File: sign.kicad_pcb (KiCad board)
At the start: 2 copper layers, 1 part

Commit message: Route 'e'
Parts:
- removed REF**: APA102C_72m_x3, apa102c_72m:APA102C_72m_x3
- added J1, J2, J3: CONN_01X02, Pin_Headers:Pin_Header_Straight_1x02, F.Cu at (28.2, 196.5)
- added U1: APA102C_x6, apa102c_72m:APA102C_72m_x6, B.Cu at (51.7, 204.4)
- added U10: APA102C_x2, apa102c_72m:APA102C_72m_x2, B.Cu at (121.1, 190.6)
- added U100: APA102C_x6, apa102c_72m:APA102C_72m_x6, B.Cu at (551.7, 79.4)
- added U101: APA102C_x4, apa102c_72m:APA102C_72m_x4, B.Cu at (551.7, 315.6)
- added U102: APA102C_x2, apa102c_72m:APA102C_72m_x2, B.Cu at (551.7, 593.3)
- added U103: APA102C_x1, apa102c_72m:APA102C_72m_x1, B.Cu at (565.6, 44.7)
- added U104: APA102C_x3, apa102c_72m:APA102C_72m_x3, B.Cu at (565.6, 322.5)
- added U105: APA102C_x5, apa102c_72m:APA102C_72m_x5, B.Cu at (565.6, 572.5)
- added U106: APA102C_x2, apa102c_72m:APA102C_72m_x2, B.Cu at (579.4, 135.0)
- added U107: APA102C_x3, apa102c_72m:APA102C_72m_x3, B.Cu at (579.4, 322.5)
- added U108: APA102C_x10, apa102c_72m:APA102C_72m_x10, B.Cu at (579.4, 537.8)
- added U109: APA102C_x9, apa102c_72m:APA102C_72m_x9, B.Cu at (593.3, 169.7)
- added U11: APA102C_x2, apa102c_72m:APA102C_72m_x2, B.Cu at (121.1, 260.0)
- added U110: APA102C_x3, apa102c_72m:APA102C_72m_x3, B.Cu at (593.3, 308.6)
- added U111: APA102C_x12, apa102c_72m:APA102C_72m_x12, B.Cu at (593.3, 523.9)
- added U112: APA102C_x16, apa102c_72m:APA102C_72m_x16, B.Cu at (607.2, 218.3)
- added U113: APA102C_x8, apa102c_72m:APA102C_72m_x8, B.Cu at (607.2, 496.1)
- added U114: APA102C_x13, apa102c_72m:APA102C_72m_x13, B.Cu at (621.1, 225.3)
- added U115: APA102C_x3, apa102c_72m:APA102C_72m_x3, B.Cu at (621.1, 489.2)
- added U116: APA102C_x6, apa102c_72m:APA102C_72m_x6, B.Cu at (635.0, 246.1)
- added U117: APA102C_x3, apa102c_72m:APA102C_72m_x3, B.Cu at (635.0, 475.3)
- added U118: APA102C_x6, apa102c_72m:APA102C_72m_x6, B.Cu at (648.9, 218.3)
- added U119: APA102C_x3, apa102c_72m:APA102C_72m_x3, B.Cu at (648.9, 461.4)
- added U12: APA102C_x2, apa102c_72m:APA102C_72m_x2, B.Cu at (135.0, 121.1)
- added U120: APA102C_x2, apa102c_72m:APA102C_72m_x2, B.Cu at (648.9, 593.3)
- added U121: APA102C_x6, apa102c_72m:APA102C_72m_x6, B.Cu at (662.8, 190.6)
- added U122: APA102C_x3, apa102c_72m:APA102C_72m_x3, B.Cu at (662.8, 461.4)
- added U123: APA102C_x6, apa102c_72m:APA102C_72m_x6, B.Cu at (662.8, 565.6)
- added U124: APA102C_x7, apa102c_72m:APA102C_72m_x7, B.Cu at (676.7, 169.7)
- added U125: APA102C_x12, apa102c_72m:APA102C_72m_x12, B.Cu at (676.7, 523.9)
- added U126: APA102C_x6, apa102c_72m:APA102C_72m_x6, B.Cu at (690.6, 148.9)
- added U127: APA102C_x11, apa102c_72m:APA102C_72m_x11, B.Cu at (690.6, 516.9)
- added U128: APA102C_x4, apa102c_72m:APA102C_72m_x4, B.Cu at (704.4, 135.0)
- added U129: APA102C_x6, apa102c_72m:APA102C_72m_x6, B.Cu at (704.4, 496.1)
- added U13: APA102C_x2, apa102c_72m:APA102C_72m_x2, B.Cu at (135.0, 190.6)
- added U130: APA102C_x2, apa102c_72m:APA102C_72m_x2, B.Cu at (718.3, 121.1)
- added U131: APA102C_x2, apa102c_72m:APA102C_72m_x2, B.Cu at (718.3, 482.2)
- added U132: APA102C_x3, apa102c_72m:APA102C_72m_x3, B.Cu at (732.2, 475.3)
- added U133: APA102C_x1, apa102c_72m:APA102C_72m_x1, B.Cu at (732.2, 600.3)
- added U134: APA102C_x3, apa102c_72m:APA102C_72m_x3, B.Cu at (746.1, 461.4)
- added U135: APA102C_x3, apa102c_72m:APA102C_72m_x3, B.Cu at (746.1, 586.4)
- added U136: APA102C_x12, apa102c_72m:APA102C_72m_x12, B.Cu at (760.0, 523.9)
- added U137: APA102C_x12, apa102c_72m:APA102C_72m_x12, B.Cu at (773.9, 523.9)
- added U138: APA102C_x9, apa102c_72m:APA102C_72m_x9, B.Cu at (787.8, 516.9)
- added U139: APA102C_x4, apa102c_72m:APA102C_72m_x4, B.Cu at (801.7, 496.1)
- added U14: APA102C_x3, apa102c_72m:APA102C_72m_x3, B.Cu at (135.0, 253.1)
- added U15: APA102C_x3, apa102c_72m:APA102C_72m_x3, B.Cu at (148.9, 128.1)
- added U16: APA102C_x3, apa102c_72m:APA102C_72m_x3, B.Cu at (148.9, 183.6)
- added U17: APA102C_x3, apa102c_72m:APA102C_72m_x3, B.Cu at (148.9, 253.1)
- added U18: APA102C_x5, apa102c_72m:APA102C_72m_x5, B.Cu at (148.9, 475.3)
- added U19: APA102C_x6, apa102c_72m:APA102C_72m_x6, B.Cu at (162.8, 148.9)
- added U2: APA102C_x8, apa102c_72m:APA102C_72m_x8, B.Cu at (65.6, 204.4)
- added U20: APA102C_x2, apa102c_72m:APA102C_72m_x2, B.Cu at (162.8, 246.1)
- added U21: APA102C_x7, apa102c_72m:APA102C_72m_x7, B.Cu at (162.8, 475.3)
- added U22: APA102C_x5, apa102c_72m:APA102C_72m_x5, B.Cu at (176.7, 155.8)
- added U23: APA102C_x7, apa102c_72m:APA102C_72m_x7, B.Cu at (176.7, 419.7)
- added U24: APA102C_x3, apa102c_72m:APA102C_72m_x3, B.Cu at (176.7, 503.1)
- added U25: APA102C_x2, apa102c_72m:APA102C_72m_x2, B.Cu at (190.6, 148.9)
- added U26: APA102C_x7, apa102c_72m:APA102C_72m_x7, B.Cu at (190.6, 405.8)
- added U27: APA102C_x2, apa102c_72m:APA102C_72m_x2, B.Cu at (190.6, 510.0)
- added U28: APA102C_x3, apa102c_72m:APA102C_72m_x3, B.Cu at (204.4, 364.2)
- added U29: APA102C_x5, apa102c_72m:APA102C_72m_x5, B.Cu at (204.4, 433.6)
- added U3: APA102C_x11, apa102c_72m:APA102C_72m_x11, B.Cu at (79.4, 197.5)
- added U30: APA102C_x2, apa102c_72m:APA102C_72m_x2, B.Cu at (204.4, 510.0)
- added U31: APA102C_x5, apa102c_72m:APA102C_72m_x5, B.Cu at (218.3, 211.4)
- added U32: APA102C_x2, apa102c_72m:APA102C_72m_x2, B.Cu at (218.3, 357.2)
- added U33: APA102C_x8, apa102c_72m:APA102C_72m_x8, B.Cu at (218.3, 468.3)
- added U34: APA102C_x9, apa102c_72m:APA102C_72m_x9, B.Cu at (232.2, 197.5)
- added U35: APA102C_x3, apa102c_72m:APA102C_72m_x3, B.Cu at (232.2, 364.2)
- added U36: APA102C_x2, apa102c_72m:APA102C_72m_x2, B.Cu at (232.2, 412.8)
- added U37: APA102C_x5, apa102c_72m:APA102C_72m_x5, B.Cu at (232.2, 475.3)
- added U38: APA102C_x11, apa102c_72m:APA102C_72m_x11, B.Cu at (246.1, 197.5)
- added U39: APA102C_x6, apa102c_72m:APA102C_72m_x6, B.Cu at (246.1, 385.0)
- added U4: APA102C_x6, apa102c_72m:APA102C_72m_x6, B.Cu at (93.3, 162.8)
- added U40: APA102C_x4, apa102c_72m:APA102C_72m_x4, B.Cu at (246.1, 496.1)
- added U41: APA102C_x5, apa102c_72m:APA102C_72m_x5, B.Cu at (260.0, 155.8)
- added U42: APA102C_x3, apa102c_72m:APA102C_72m_x3, B.Cu at (260.0, 253.1)
- added U43: APA102C_x4, apa102c_72m:APA102C_72m_x4, B.Cu at (260.0, 385.0)
- added U44: APA102C_x6, apa102c_72m:APA102C_72m_x6, B.Cu at (260.0, 482.2)
- added U45: APA102C_x4, apa102c_72m:APA102C_72m_x4, B.Cu at (273.9, 135.0)
- added U46: APA102C_x3, apa102c_72m:APA102C_72m_x3, B.Cu at (273.9, 253.1)
- added U47: APA102C_x4, apa102c_72m:APA102C_72m_x4, B.Cu at (273.9, 454.4)
- added U48: APA102C_x2, apa102c_72m:APA102C_72m_x2, B.Cu at (273.9, 510.0)
- added U49: APA102C_x3, apa102c_72m:APA102C_72m_x3, B.Cu at (287.8, 128.1)
- added U5: APA102C_x3, apa102c_72m:APA102C_72m_x3, B.Cu at (93.3, 253.1)
- added U50: APA102C_x2, apa102c_72m:APA102C_72m_x2, B.Cu at (287.8, 246.1)
- added U51: APA102C_x2, apa102c_72m:APA102C_72m_x2, B.Cu at (287.8, 440.6)
- added U52: APA102C_x3, apa102c_72m:APA102C_72m_x3, B.Cu at (301.7, 128.1)
- added U53: APA102C_x3, apa102c_72m:APA102C_72m_x3, B.Cu at (301.7, 239.2)
- added U54: APA102C_x3, apa102c_72m:APA102C_72m_x3, B.Cu at (301.7, 641.9)
- added U55: APA102C_x3, apa102c_72m:APA102C_72m_x3, B.Cu at (315.6, 141.9)
- added U56: APA102C_x7, apa102c_72m:APA102C_72m_x7, B.Cu at (315.6, 225.3)
- added U57: APA102C_x4, apa102c_72m:APA102C_72m_x4, B.Cu at (315.6, 648.9)
- added U58: APA102C_x12, apa102c_72m:APA102C_72m_x12, B.Cu at (329.4, 190.6)
- added U59: APA102C_x3, apa102c_72m:APA102C_72m_x3, B.Cu at (329.4, 655.8)
- added U6: APA102C_x3, apa102c_72m:APA102C_72m_x3, B.Cu at (107.2, 128.1)
- added U60: APA102C_x14, apa102c_72m:APA102C_72m_x14, B.Cu at (343.3, 148.9)
- added U61: APA102C_x3, apa102c_72m:APA102C_72m_x3, B.Cu at (343.3, 655.8)
- added U62: APA102C_x10, apa102c_72m:APA102C_72m_x10, B.Cu at (357.2, 107.2)
- added U63: APA102C_x4, apa102c_72m:APA102C_72m_x4, B.Cu at (357.2, 635.0)
- added U64: APA102C_x6, apa102c_72m:APA102C_72m_x6, B.Cu at (371.1, 79.4)
- added U65: APA102C_x9, apa102c_72m:APA102C_72m_x9, B.Cu at (371.1, 600.3)
- added U66: APA102C_x1, apa102c_72m:APA102C_72m_x1, B.Cu at (385.0, 44.7)
- added U67: APA102C_x13, apa102c_72m:APA102C_72m_x13, B.Cu at (385.0, 558.6)
- added U68: APA102C_x5, apa102c_72m:APA102C_72m_x5, B.Cu at (398.9, 211.4)
- added U69: APA102C_x13, apa102c_72m:APA102C_72m_x13, B.Cu at (398.9, 530.8)
- added U7: APA102C_x2, apa102c_72m:APA102C_72m_x2, B.Cu at (107.2, 190.6)
- added U70: APA102C_x9, apa102c_72m:APA102C_72m_x9, B.Cu at (412.8, 197.5)
- added U71: APA102C_x2, apa102c_72m:APA102C_72m_x2, B.Cu at (412.8, 398.9)
- added U72: APA102C_x8, apa102c_72m:APA102C_72m_x8, B.Cu at (412.8, 496.1)
- added U73: APA102C_x11, apa102c_72m:APA102C_72m_x11, B.Cu at (426.7, 197.5)
- added U74: APA102C_x3, apa102c_72m:APA102C_72m_x3, B.Cu at (426.7, 391.9)
- added U75: APA102C_x3, apa102c_72m:APA102C_72m_x3, B.Cu at (426.7, 461.4)
- added U76: APA102C_x5, apa102c_72m:APA102C_72m_x5, B.Cu at (440.6, 155.8)
- added U77: APA102C_x3, apa102c_72m:APA102C_72m_x3, B.Cu at (440.6, 253.1)
- added U78: APA102C_x2, apa102c_72m:APA102C_72m_x2, B.Cu at (440.6, 385.0)
- added U79: APA102C_x4, apa102c_72m:APA102C_72m_x4, B.Cu at (454.4, 135.0)
- added U8: APA102C_x3, apa102c_72m:APA102C_72m_x3, B.Cu at (107.2, 253.1)
- added U80: APA102C_x3, apa102c_72m:APA102C_72m_x3, B.Cu at (454.4, 253.1)
- added U81: APA102C_x2, apa102c_72m:APA102C_72m_x2, B.Cu at (454.4, 593.3)
- added U82: APA102C_x3, apa102c_72m:APA102C_72m_x3, B.Cu at (468.3, 128.1)
- added U83: APA102C_x2, apa102c_72m:APA102C_72m_x2, B.Cu at (468.3, 246.1)
- added U84: APA102C_x5, apa102c_72m:APA102C_72m_x5, B.Cu at (468.3, 572.5)
- added U85: APA102C_x3, apa102c_72m:APA102C_72m_x3, B.Cu at (482.2, 128.1)
- added U86: APA102C_x3, apa102c_72m:APA102C_72m_x3, B.Cu at (482.2, 239.2)
- added U87: APA102C_x10, apa102c_72m:APA102C_72m_x10, B.Cu at (482.2, 537.8)
- added U88: APA102C_x3, apa102c_72m:APA102C_72m_x3, B.Cu at (496.1, 141.9)
- added U89: APA102C_x7, apa102c_72m:APA102C_72m_x7, B.Cu at (496.1, 225.3)
- added U9: APA102C_x3, apa102c_72m:APA102C_72m_x3, B.Cu at (121.1, 128.1)
- added U90: APA102C_x12, apa102c_72m:APA102C_72m_x12, B.Cu at (496.1, 523.9)
- added U91: APA102C_x12, apa102c_72m:APA102C_72m_x12, B.Cu at (510.0, 190.6)
- added U92: APA102C_x2, apa102c_72m:APA102C_72m_x2, B.Cu at (510.0, 398.9)
- added U93: APA102C_x8, apa102c_72m:APA102C_72m_x8, B.Cu at (510.0, 496.1)
- added U94: APA102C_x14, apa102c_72m:APA102C_72m_x14, B.Cu at (523.9, 148.9)
- added U95: APA102C_x3, apa102c_72m:APA102C_72m_x3, B.Cu at (523.9, 391.9)
- added U96: APA102C_x3, apa102c_72m:APA102C_72m_x3, B.Cu at (523.9, 461.4)
- added U97: APA102C_x10, apa102c_72m:APA102C_72m_x10, B.Cu at (537.8, 107.2)
- added U98: APA102C_x3, apa102c_72m:APA102C_72m_x3, B.Cu at (537.8, 308.6)
- added U99: APA102C_x2, apa102c_72m:APA102C_72m_x2, B.Cu at (537.8, 385.0)
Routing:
- net Net-(U20-Pad8): track 0.00 -> 198.2 mm
- net Net-(U20-Pad7): track 0.00 -> 191.6 mm
- net Net-(U20-Pad6): track 0.00 -> 183.7 mm
- net Net-(U20-Pad5): track 0.00 -> 175.3 mm
- net Net-(U16-Pad4): track 0.00 -> 59.6 mm
- net Net-(U2-Pad5): track 0.00 -> 58.5 mm
- net Net-(U16-Pad3): track 0.00 -> 58.1 mm
- net Net-(U16-Pad2): track 0.00 -> 57.4 mm
- net Net-(U16-Pad1): track 0.00 -> 54.2 mm
- net Net-(U2-Pad6): track 0.00 -> 50.8 mm
- net Net-(U12-Pad8): track 0.00 -> 47.2 mm
- net Net-(U4-Pad5): track 0.00 -> 46.3 mm
- net Net-(U1-Pad8): track 0.00 -> 46.2 mm
- net Net-(U22-Pad5): track 0.00 -> 46.0 mm
- net Net-(U2-Pad7): track 0.00 -> 44.6 mm
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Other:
- net class Default: clearance 0.2 -> 0.6; trace_width 0.25 -> 2
- net class Signal added: clearance 0.6, trace_width 1, via_dia 0.6, via_drill 0.4
- rule trace_clearance: 0.2 -> 0.6

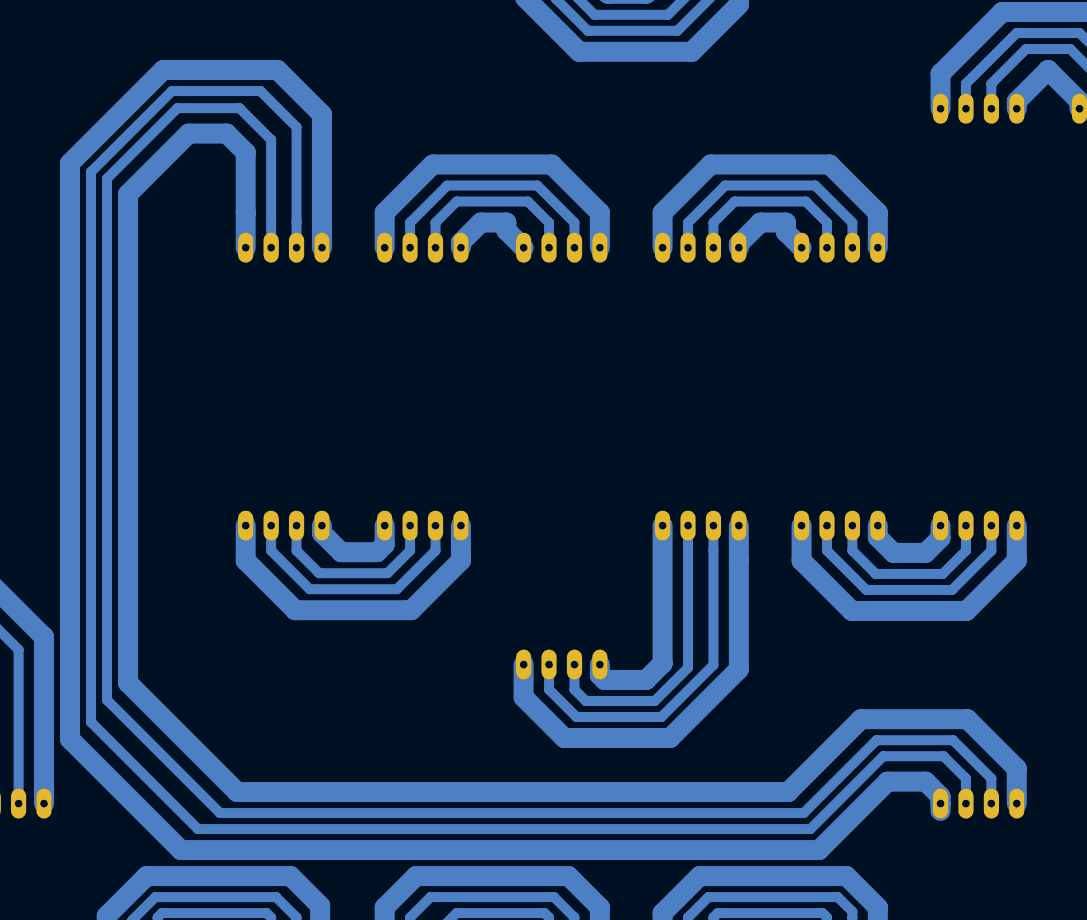
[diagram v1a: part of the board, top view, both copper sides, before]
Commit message: nets for 'i'
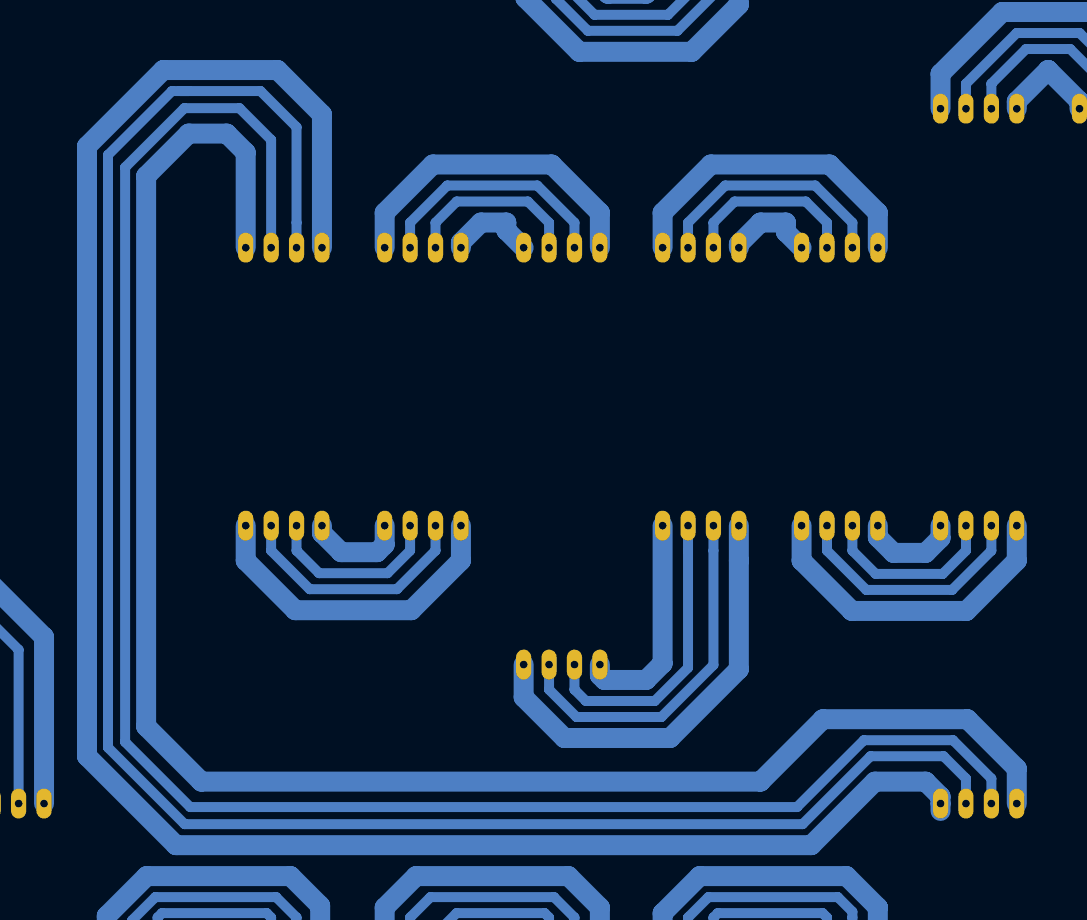
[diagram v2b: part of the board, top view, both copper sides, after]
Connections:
- U81 pad 5: (no net) -> Net-(U81-Pad5)
- U81 pad 6: (no net) -> Net-(U81-Pad6)
- U81 pad 7: (no net) -> Net-(U81-Pad7)
- U81 pad 8: (no net) -> Net-(U81-Pad8)
- U84 pad 1: (no net) -> Net-(U81-Pad5)
- U84 pad 2: (no net) -> Net-(U81-Pad6)
- U84 pad 3: (no net) -> Net-(U81-Pad7)
- U84 pad 4: (no net) -> Net-(U81-Pad8)
- U84 pad 5: (no net) -> Net-(U84-Pad5)
- U84 pad 6: (no net) -> Net-(U84-Pad6)
- U84 pad 7: (no net) -> Net-(U84-Pad7)
- U84 pad 8: (no net) -> Net-(U84-Pad8)
- U87 pad 1: (no net) -> Net-(U84-Pad5)
- U87 pad 2: (no net) -> Net-(U84-Pad6)
- U87 pad 3: (no net) -> Net-(U84-Pad7)
- U87 pad 4: (no net) -> Net-(U84-Pad8)
- U87 pad 5: (no net) -> Net-(U87-Pad5)
- U87 pad 6: (no net) -> Net-(U87-Pad6)
- U87 pad 7: (no net) -> Net-(U87-Pad7)
- U87 pad 8: (no net) -> Net-(U87-Pad8)
- U90 pad 1: (no net) -> Net-(U87-Pad5)
- U90 pad 2: (no net) -> Net-(U87-Pad6)
- U90 pad 3: (no net) -> Net-(U87-Pad7)
- U90 pad 4: (no net) -> Net-(U87-Pad8)
- U90 pad 5: (no net) -> Net-(U90-Pad5)
- U90 pad 6: (no net) -> Net-(U90-Pad6)
- U90 pad 7: (no net) -> Net-(U90-Pad7)
- U90 pad 8: (no net) -> Net-(U90-Pad8)
- U93 pad 1: (no net) -> Net-(U90-Pad5)
- U93 pad 2: (no net) -> Net-(U90-Pad6)
- U93 pad 3: (no net) -> Net-(U90-Pad7)
- U93 pad 4: (no net) -> Net-(U90-Pad8)
- U93 pad 5: (no net) -> Net-(U93-Pad5)
- U93 pad 6: (no net) -> Net-(U93-Pad6)
- U93 pad 7: (no net) -> Net-(U93-Pad7)
- U93 pad 8: (no net) -> Net-(U93-Pad8)
- U96 pad 1: (no net) -> Net-(U93-Pad5)
- U96 pad 2: (no net) -> Net-(U93-Pad6)
- U96 pad 3: (no net) -> Net-(U93-Pad7)
- U96 pad 4: (no net) -> Net-(U93-Pad8)
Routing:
- net Net-(U20-Pad8): track 198.2 -> 196.4 mm
- net Net-(U20-Pad7): track 191.6 -> 190.2 mm
- net Net-(U20-Pad6): track 183.7 -> 182.7 mm
- net Net-(U20-Pad5): track 175.3 -> 174.4 mm

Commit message: Add cuts layer.
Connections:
- J1 pad 1: +5V -> GND
- J1 pad 2: GND -> +5V
- U1 pad 1: +5V -> GND
- U1 pad 4: GND -> +5V
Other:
- board outline added: 767.9 x 642.9 mm

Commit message: Update edge cuts
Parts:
- moved J2 10.1 mm to (25.7, 206.2)
- moved J1 8.34 mm to (25.9, 188.5)

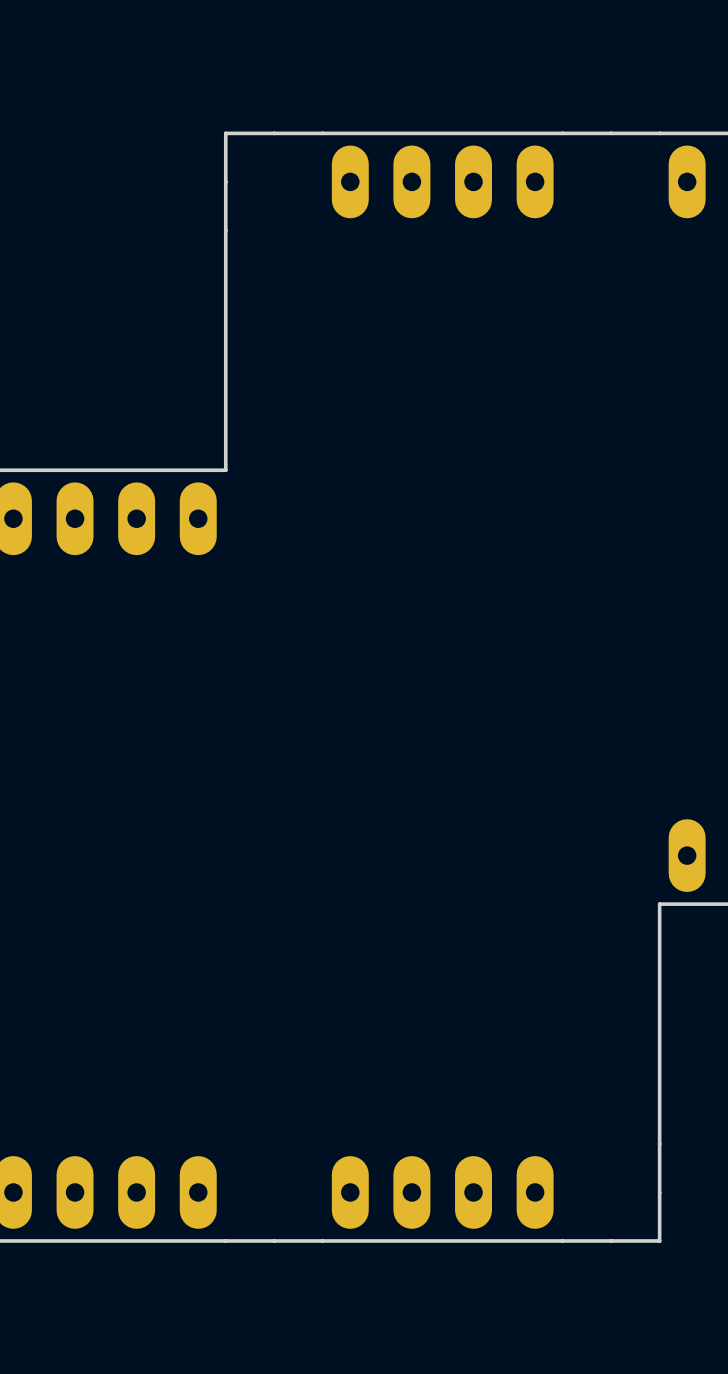
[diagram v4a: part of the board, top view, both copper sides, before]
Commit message: Wire up some more letters.
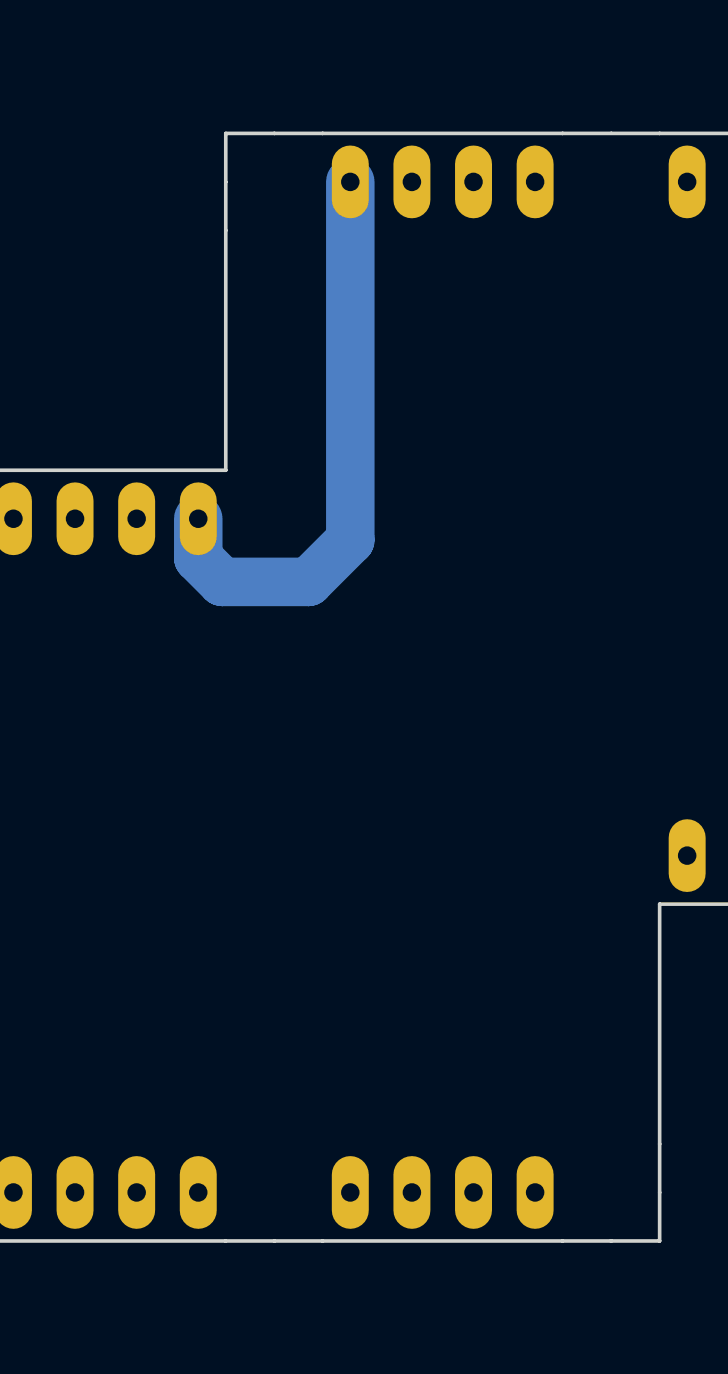
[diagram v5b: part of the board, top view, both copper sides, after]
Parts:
- turned U74 to 270 degrees
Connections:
- U100 pad 1: (no net) -> Net-(U100-Pad1)
- U100 pad 2: (no net) -> Net-(U100-Pad2)
- U100 pad 3: (no net) -> Net-(U100-Pad3)
- U100 pad 4: (no net) -> Net-(U100-Pad4)
- U100 pad 5: (no net) -> Net-(U100-Pad5)
- U100 pad 6: (no net) -> Net-(U100-Pad6)
- U100 pad 7: (no net) -> Net-(U100-Pad7)
- U100 pad 8: (no net) -> Net-(U100-Pad8)
- U103 pad 1: (no net) -> Net-(U100-Pad5)
- U103 pad 2: (no net) -> Net-(U100-Pad6)
- U103 pad 3: (no net) -> Net-(U100-Pad7)
- U103 pad 4: (no net) -> Net-(U100-Pad8)
- U103 pad 5: (no net) -> Net-(U103-Pad5)
- U103 pad 6: (no net) -> Net-(U103-Pad6)
- U103 pad 7: (no net) -> Net-(U103-Pad7)
- U103 pad 8: (no net) -> Net-(U103-Pad8)
- U31 pad 1: (no net) -> GND
- U31 pad 4: (no net) -> +5V
- U31 pad 5: (no net) -> Net-(U31-Pad5)
- U31 pad 6: (no net) -> Net-(U31-Pad6)
- U31 pad 7: (no net) -> Net-(U31-Pad7)
- U31 pad 8: (no net) -> Net-(U31-Pad8)
- U34 pad 1: (no net) -> Net-(U31-Pad5)
- U34 pad 2: (no net) -> Net-(U31-Pad6)
- U34 pad 3: (no net) -> Net-(U31-Pad7)
- U34 pad 4: (no net) -> Net-(U31-Pad8)
- U34 pad 5: (no net) -> Net-(U34-Pad5)
- U34 pad 6: (no net) -> Net-(U34-Pad6)
- U34 pad 7: (no net) -> Net-(U34-Pad7)
- U34 pad 8: (no net) -> Net-(U34-Pad8)
- U38 pad 1: (no net) -> Net-(U34-Pad5)
- U38 pad 2: (no net) -> Net-(U34-Pad6)
- U38 pad 3: (no net) -> Net-(U34-Pad7)
- U38 pad 4: (no net) -> Net-(U34-Pad8)
- U38 pad 5: (no net) -> Net-(U38-Pad5)
- U38 pad 6: (no net) -> Net-(U38-Pad6)
- U38 pad 7: (no net) -> Net-(U38-Pad7)
- U38 pad 8: (no net) -> Net-(U38-Pad8)
- U41 pad 1: (no net) -> Net-(U41-Pad1)
- U41 pad 2: (no net) -> Net-(U41-Pad2)
- U41 pad 3: (no net) -> Net-(U41-Pad3)
- U41 pad 4: (no net) -> Net-(U41-Pad4)
- U42 pad 1: (no net) -> Net-(U38-Pad5)
- U42 pad 2: (no net) -> Net-(U38-Pad6)
- U42 pad 3: (no net) -> Net-(U38-Pad7)
- U42 pad 4: (no net) -> Net-(U38-Pad8)
- U42 pad 5: (no net) -> Net-(U42-Pad5)
- U42 pad 6: (no net) -> Net-(U42-Pad6)
- U42 pad 7: (no net) -> Net-(U42-Pad7)
- U42 pad 8: (no net) -> Net-(U42-Pad8)
- U45 pad 1: (no net) -> Net-(U45-Pad1)
- U45 pad 2: (no net) -> Net-(U45-Pad2)
- U45 pad 3: (no net) -> Net-(U45-Pad3)
- U45 pad 4: (no net) -> Net-(U45-Pad4)
- U45 pad 5: (no net) -> Net-(U41-Pad1)
- U45 pad 6: (no net) -> Net-(U41-Pad2)
- U45 pad 7: (no net) -> Net-(U41-Pad3)
- U45 pad 8: (no net) -> Net-(U41-Pad4)
- U46 pad 1: (no net) -> Net-(U42-Pad5)
- U46 pad 2: (no net) -> Net-(U42-Pad6)
- U46 pad 3: (no net) -> Net-(U42-Pad7)
- U46 pad 4: (no net) -> Net-(U42-Pad8)
- U46 pad 5: (no net) -> Net-(U46-Pad5)
- U46 pad 6: (no net) -> Net-(U46-Pad6)
- U46 pad 7: (no net) -> Net-(U46-Pad7)
- U46 pad 8: (no net) -> Net-(U46-Pad8)
- U49 pad 1: (no net) -> Net-(U49-Pad1)
- U49 pad 2: (no net) -> Net-(U49-Pad2)
- U49 pad 3: (no net) -> Net-(U49-Pad3)
- U49 pad 4: (no net) -> Net-(U49-Pad4)
- U49 pad 5: (no net) -> Net-(U45-Pad1)
- U49 pad 6: (no net) -> Net-(U45-Pad2)
- U49 pad 7: (no net) -> Net-(U45-Pad3)
- U49 pad 8: (no net) -> Net-(U45-Pad4)
- U50 pad 1: (no net) -> Net-(U46-Pad5)
- U50 pad 2: (no net) -> Net-(U46-Pad6)
- U50 pad 3: (no net) -> Net-(U46-Pad7)
- U50 pad 4: (no net) -> Net-(U46-Pad8)
- U50 pad 5: (no net) -> Net-(U50-Pad5)
- U50 pad 6: (no net) -> Net-(U50-Pad6)
- U50 pad 7: (no net) -> Net-(U50-Pad7)
- U50 pad 8: (no net) -> Net-(U50-Pad8)
- U52 pad 1: (no net) -> Net-(U52-Pad1)
- U52 pad 2: (no net) -> Net-(U52-Pad2)
- U52 pad 3: (no net) -> Net-(U52-Pad3)
- U52 pad 4: (no net) -> Net-(U52-Pad4)
- U52 pad 5: (no net) -> Net-(U49-Pad1)
- U52 pad 6: (no net) -> Net-(U49-Pad2)
- U52 pad 7: (no net) -> Net-(U49-Pad3)
- U52 pad 8: (no net) -> Net-(U49-Pad4)
- U53 pad 1: (no net) -> Net-(U50-Pad5)
- U53 pad 2: (no net) -> Net-(U50-Pad6)
- U53 pad 3: (no net) -> Net-(U50-Pad7)
- U53 pad 4: (no net) -> Net-(U50-Pad8)
- U53 pad 5: (no net) -> Net-(U53-Pad5)
- U53 pad 6: (no net) -> Net-(U53-Pad6)
- U53 pad 7: (no net) -> Net-(U53-Pad7)
- U53 pad 8: (no net) -> Net-(U53-Pad8)
- U54 pad 5: (no net) -> Net-(U54-Pad5)
- U54 pad 6: (no net) -> Net-(U54-Pad6)
- U54 pad 7: (no net) -> Net-(U54-Pad7)
- U54 pad 8: (no net) -> Net-(U54-Pad8)
- U55 pad 1: (no net) -> Net-(U55-Pad1)
- U55 pad 2: (no net) -> Net-(U55-Pad2)
- U55 pad 3: (no net) -> Net-(U55-Pad3)
- U55 pad 4: (no net) -> Net-(U55-Pad4)
- U55 pad 5: (no net) -> Net-(U52-Pad1)
- U55 pad 6: (no net) -> Net-(U52-Pad2)
- U55 pad 7: (no net) -> Net-(U52-Pad3)
- U55 pad 8: (no net) -> Net-(U52-Pad4)
- U56 pad 1: (no net) -> Net-(U53-Pad5)
- U56 pad 2: (no net) -> Net-(U53-Pad6)
- U56 pad 3: (no net) -> Net-(U53-Pad7)
- U56 pad 4: (no net) -> Net-(U53-Pad8)
- U56 pad 5: (no net) -> Net-(U56-Pad5)
- U56 pad 6: (no net) -> Net-(U56-Pad6)
- U56 pad 7: (no net) -> Net-(U56-Pad7)
- U56 pad 8: (no net) -> Net-(U56-Pad8)
- U57 pad 1: (no net) -> Net-(U54-Pad5)
- U57 pad 2: (no net) -> Net-(U54-Pad6)
- U57 pad 3: (no net) -> Net-(U54-Pad7)
- U57 pad 4: (no net) -> Net-(U54-Pad8)
- U57 pad 5: (no net) -> Net-(U57-Pad5)
- U57 pad 6: (no net) -> Net-(U57-Pad6)
- U57 pad 7: (no net) -> Net-(U57-Pad7)
- U57 pad 8: (no net) -> Net-(U57-Pad8)
- U58 pad 1: (no net) -> Net-(U56-Pad5)
- U58 pad 2: (no net) -> Net-(U56-Pad6)
- U58 pad 3: (no net) -> Net-(U56-Pad7)
- U58 pad 4: (no net) -> Net-(U56-Pad8)
- U58 pad 5: (no net) -> Net-(U58-Pad5)
- U58 pad 6: (no net) -> Net-(U58-Pad6)
- U58 pad 7: (no net) -> Net-(U58-Pad7)
- U58 pad 8: (no net) -> Net-(U58-Pad8)
- U59 pad 1: (no net) -> Net-(U57-Pad5)
- U59 pad 2: (no net) -> Net-(U57-Pad6)
- U59 pad 3: (no net) -> Net-(U57-Pad7)
- U59 pad 4: (no net) -> Net-(U57-Pad8)
- U59 pad 5: (no net) -> Net-(U59-Pad5)
- U59 pad 6: (no net) -> Net-(U59-Pad6)
- U59 pad 7: (no net) -> Net-(U59-Pad7)
- U59 pad 8: (no net) -> Net-(U59-Pad8)
- U60 pad 1: (no net) -> Net-(U58-Pad5)
- U60 pad 2: (no net) -> Net-(U58-Pad6)
- U60 pad 3: (no net) -> Net-(U58-Pad7)
- U60 pad 4: (no net) -> Net-(U58-Pad8)
- U60 pad 5: (no net) -> Net-(U60-Pad5)
- U60 pad 6: (no net) -> Net-(U60-Pad6)
- U60 pad 7: (no net) -> Net-(U60-Pad7)
- U60 pad 8: (no net) -> Net-(U60-Pad8)
- U61 pad 1: (no net) -> Net-(U59-Pad5)
- U61 pad 2: (no net) -> Net-(U59-Pad6)
- U61 pad 3: (no net) -> Net-(U59-Pad7)
- U61 pad 4: (no net) -> Net-(U59-Pad8)
- U61 pad 5: (no net) -> Net-(U61-Pad5)
- U61 pad 6: (no net) -> Net-(U61-Pad6)
- U61 pad 7: (no net) -> Net-(U61-Pad7)
- U61 pad 8: (no net) -> Net-(U61-Pad8)
- U62 pad 1: (no net) -> Net-(U60-Pad5)
- U62 pad 2: (no net) -> Net-(U60-Pad6)
- U62 pad 3: (no net) -> Net-(U60-Pad7)
- U62 pad 4: (no net) -> Net-(U60-Pad8)
- U62 pad 5: (no net) -> Net-(U62-Pad5)
- U62 pad 6: (no net) -> Net-(U62-Pad6)
- U62 pad 7: (no net) -> Net-(U62-Pad7)
- U62 pad 8: (no net) -> Net-(U62-Pad8)
- U63 pad 1: (no net) -> Net-(U61-Pad5)
- U63 pad 2: (no net) -> Net-(U61-Pad6)
- U63 pad 3: (no net) -> Net-(U61-Pad7)
- U63 pad 4: (no net) -> Net-(U61-Pad8)
- U63 pad 5: (no net) -> Net-(U63-Pad5)
- U63 pad 6: (no net) -> Net-(U63-Pad6)
- U63 pad 7: (no net) -> Net-(U63-Pad7)
- U63 pad 8: (no net) -> Net-(U63-Pad8)
- U64 pad 1: (no net) -> Net-(U62-Pad5)
- U64 pad 2: (no net) -> Net-(U62-Pad6)
- U64 pad 3: (no net) -> Net-(U62-Pad7)
- U64 pad 4: (no net) -> Net-(U62-Pad8)
- U64 pad 5: (no net) -> Net-(U64-Pad5)
- U64 pad 6: (no net) -> Net-(U64-Pad6)
- U64 pad 7: (no net) -> Net-(U64-Pad7)
- U64 pad 8: (no net) -> Net-(U64-Pad8)
- U65 pad 1: (no net) -> Net-(U63-Pad5)
- U65 pad 2: (no net) -> Net-(U63-Pad6)
- U65 pad 3: (no net) -> Net-(U63-Pad7)
- U65 pad 4: (no net) -> Net-(U63-Pad8)
- U65 pad 5: (no net) -> Net-(U65-Pad5)
- U65 pad 6: (no net) -> Net-(U65-Pad6)
- U65 pad 7: (no net) -> Net-(U65-Pad7)
- U65 pad 8: (no net) -> Net-(U65-Pad8)
- U66 pad 1: (no net) -> Net-(U64-Pad5)
- U66 pad 2: (no net) -> Net-(U64-Pad6)
- U66 pad 3: (no net) -> Net-(U64-Pad7)
- U66 pad 4: (no net) -> Net-(U64-Pad8)
- U66 pad 5: (no net) -> Net-(U55-Pad1)
- U66 pad 6: (no net) -> Net-(U55-Pad2)
- U66 pad 7: (no net) -> Net-(U55-Pad3)
- U66 pad 8: (no net) -> Net-(U55-Pad4)
- U67 pad 1: (no net) -> Net-(U65-Pad5)
- U67 pad 2: (no net) -> Net-(U65-Pad6)
- U67 pad 3: (no net) -> Net-(U65-Pad7)
- U67 pad 4: (no net) -> Net-(U65-Pad8)
- U67 pad 5: (no net) -> Net-(U67-Pad5)
- U67 pad 6: (no net) -> Net-(U67-Pad6)
- U67 pad 7: (no net) -> Net-(U67-Pad7)
- U67 pad 8: (no net) -> Net-(U67-Pad8)
- U68 pad 1: (no net) -> GND
- U68 pad 4: (no net) -> +5V
- U68 pad 5: (no net) -> Net-(U68-Pad5)
- U68 pad 6: (no net) -> Net-(U68-Pad6)
- U68 pad 7: (no net) -> Net-(U68-Pad7)
- U68 pad 8: (no net) -> Net-(U68-Pad8)
- U69 pad 1: (no net) -> Net-(U67-Pad5)
- U69 pad 2: (no net) -> Net-(U67-Pad6)
- U69 pad 3: (no net) -> Net-(U67-Pad7)
- U69 pad 4: (no net) -> Net-(U67-Pad8)
- U69 pad 5: (no net) -> Net-(U69-Pad5)
- U69 pad 6: (no net) -> Net-(U69-Pad6)
- U69 pad 7: (no net) -> Net-(U69-Pad7)
- U69 pad 8: (no net) -> Net-(U69-Pad8)
- U70 pad 1: (no net) -> Net-(U68-Pad5)
- U70 pad 2: (no net) -> Net-(U68-Pad6)
- U70 pad 3: (no net) -> Net-(U68-Pad7)
- U70 pad 4: (no net) -> Net-(U68-Pad8)
- U70 pad 5: (no net) -> Net-(U70-Pad5)
- U70 pad 6: (no net) -> Net-(U70-Pad6)
- U70 pad 7: (no net) -> Net-(U70-Pad7)
- U70 pad 8: (no net) -> Net-(U70-Pad8)
- U71 pad 5: (no net) -> Net-(U71-Pad5)
- U71 pad 6: (no net) -> Net-(U71-Pad6)
- U71 pad 7: (no net) -> Net-(U71-Pad7)
- U71 pad 8: (no net) -> Net-(U71-Pad8)
- U72 pad 1: (no net) -> Net-(U69-Pad5)
- U72 pad 2: (no net) -> Net-(U69-Pad6)
- U72 pad 3: (no net) -> Net-(U69-Pad7)
- U72 pad 4: (no net) -> Net-(U69-Pad8)
- U72 pad 5: (no net) -> Net-(U72-Pad5)
- U72 pad 6: (no net) -> Net-(U72-Pad6)
- U72 pad 7: (no net) -> Net-(U72-Pad7)
- U72 pad 8: (no net) -> Net-(U72-Pad8)
- U73 pad 1: (no net) -> Net-(U70-Pad5)
- U73 pad 2: (no net) -> Net-(U70-Pad6)
- U73 pad 3: (no net) -> Net-(U70-Pad7)
- U73 pad 4: (no net) -> Net-(U70-Pad8)
- U73 pad 5: (no net) -> Net-(U73-Pad5)
- U73 pad 6: (no net) -> Net-(U73-Pad6)
- U73 pad 7: (no net) -> Net-(U73-Pad7)
- U73 pad 8: (no net) -> Net-(U73-Pad8)
- U74 pad 1: (no net) -> Net-(U71-Pad5)
- U74 pad 2: (no net) -> Net-(U71-Pad6)
- U74 pad 3: (no net) -> Net-(U71-Pad7)
- U74 pad 4: (no net) -> Net-(U71-Pad8)
- U74 pad 5: (no net) -> Net-(U74-Pad5)
- U74 pad 6: (no net) -> Net-(U74-Pad6)
- U74 pad 7: (no net) -> Net-(U74-Pad7)
- U74 pad 8: (no net) -> Net-(U74-Pad8)
- U75 pad 1: (no net) -> Net-(U72-Pad5)
- U75 pad 2: (no net) -> Net-(U72-Pad6)
- U75 pad 3: (no net) -> Net-(U72-Pad7)
- U75 pad 4: (no net) -> Net-(U72-Pad8)
- U76 pad 1: (no net) -> Net-(U76-Pad1)
- U76 pad 2: (no net) -> Net-(U76-Pad2)
- U76 pad 3: (no net) -> Net-(U76-Pad3)
- U76 pad 4: (no net) -> Net-(U76-Pad4)
- U77 pad 1: (no net) -> Net-(U73-Pad5)
- U77 pad 2: (no net) -> Net-(U73-Pad6)
- U77 pad 3: (no net) -> Net-(U73-Pad7)
- U77 pad 4: (no net) -> Net-(U73-Pad8)
- U77 pad 5: (no net) -> Net-(U77-Pad5)
- U77 pad 6: (no net) -> Net-(U77-Pad6)
- U77 pad 7: (no net) -> Net-(U77-Pad7)
- U77 pad 8: (no net) -> Net-(U77-Pad8)
- U78 pad 1: (no net) -> Net-(U74-Pad5)
- U78 pad 2: (no net) -> Net-(U74-Pad6)
- U78 pad 3: (no net) -> Net-(U74-Pad7)
- U78 pad 4: (no net) -> Net-(U74-Pad8)
- U79 pad 1: (no net) -> Net-(U79-Pad1)
- U79 pad 2: (no net) -> Net-(U79-Pad2)
- U79 pad 3: (no net) -> Net-(U79-Pad3)
- U79 pad 4: (no net) -> Net-(U79-Pad4)
- U79 pad 5: (no net) -> Net-(U76-Pad1)
- U79 pad 6: (no net) -> Net-(U76-Pad2)
- U79 pad 7: (no net) -> Net-(U76-Pad3)
- U79 pad 8: (no net) -> Net-(U76-Pad4)
- U80 pad 1: (no net) -> Net-(U77-Pad5)
- U80 pad 2: (no net) -> Net-(U77-Pad6)
- U80 pad 3: (no net) -> Net-(U77-Pad7)
- U80 pad 4: (no net) -> Net-(U77-Pad8)
- U80 pad 5: (no net) -> Net-(U80-Pad5)
- U80 pad 6: (no net) -> Net-(U80-Pad6)
- U80 pad 7: (no net) -> Net-(U80-Pad7)
- U80 pad 8: (no net) -> Net-(U80-Pad8)
- U82 pad 1: (no net) -> Net-(U82-Pad1)
- U82 pad 2: (no net) -> Net-(U82-Pad2)
- U82 pad 3: (no net) -> Net-(U82-Pad3)
- U82 pad 4: (no net) -> Net-(U82-Pad4)
- U82 pad 5: (no net) -> Net-(U79-Pad1)
- U82 pad 6: (no net) -> Net-(U79-Pad2)
- U82 pad 7: (no net) -> Net-(U79-Pad3)
- U82 pad 8: (no net) -> Net-(U79-Pad4)
- U83 pad 1: (no net) -> Net-(U80-Pad5)
- U83 pad 2: (no net) -> Net-(U80-Pad6)
- U83 pad 3: (no net) -> Net-(U80-Pad7)
- U83 pad 4: (no net) -> Net-(U80-Pad8)
- U83 pad 5: (no net) -> Net-(U83-Pad5)
- U83 pad 6: (no net) -> Net-(U83-Pad6)
- U83 pad 7: (no net) -> Net-(U83-Pad7)
- U83 pad 8: (no net) -> Net-(U83-Pad8)
- U85 pad 1: (no net) -> Net-(U85-Pad1)
- U85 pad 2: (no net) -> Net-(U85-Pad2)
- U85 pad 3: (no net) -> Net-(U85-Pad3)
- U85 pad 4: (no net) -> Net-(U85-Pad4)
- U85 pad 5: (no net) -> Net-(U82-Pad1)
- U85 pad 6: (no net) -> Net-(U82-Pad2)
- U85 pad 7: (no net) -> Net-(U82-Pad3)
- U85 pad 8: (no net) -> Net-(U82-Pad4)
- U86 pad 1: (no net) -> Net-(U83-Pad5)
- U86 pad 2: (no net) -> Net-(U83-Pad6)
- U86 pad 3: (no net) -> Net-(U83-Pad7)
- U86 pad 4: (no net) -> Net-(U83-Pad8)
- U86 pad 5: (no net) -> Net-(U86-Pad5)
- U86 pad 6: (no net) -> Net-(U86-Pad6)
- U86 pad 7: (no net) -> Net-(U86-Pad7)
- U86 pad 8: (no net) -> Net-(U86-Pad8)
- U88 pad 1: (no net) -> Net-(U103-Pad5)
- U88 pad 2: (no net) -> Net-(U103-Pad6)
- U88 pad 3: (no net) -> Net-(U103-Pad7)
- U88 pad 4: (no net) -> Net-(U103-Pad8)
- U88 pad 5: (no net) -> Net-(U85-Pad1)
- U88 pad 6: (no net) -> Net-(U85-Pad2)
- U88 pad 7: (no net) -> Net-(U85-Pad3)
- U88 pad 8: (no net) -> Net-(U85-Pad4)
- U89 pad 1: (no net) -> Net-(U86-Pad5)
- U89 pad 2: (no net) -> Net-(U86-Pad6)
- U89 pad 3: (no net) -> Net-(U86-Pad7)
- U89 pad 4: (no net) -> Net-(U86-Pad8)
- U89 pad 5: (no net) -> Net-(U89-Pad5)
- U89 pad 6: (no net) -> Net-(U89-Pad6)
- U89 pad 7: (no net) -> Net-(U89-Pad7)
- U89 pad 8: (no net) -> Net-(U89-Pad8)
- U91 pad 1: (no net) -> Net-(U89-Pad5)
- U91 pad 2: (no net) -> Net-(U89-Pad6)
- U91 pad 3: (no net) -> Net-(U89-Pad7)
- U91 pad 4: (no net) -> Net-(U89-Pad8)
- U91 pad 5: (no net) -> Net-(U91-Pad5)
- U91 pad 6: (no net) -> Net-(U91-Pad6)
- U91 pad 7: (no net) -> Net-(U91-Pad7)
- U91 pad 8: (no net) -> Net-(U91-Pad8)
- U92 pad 5: (no net) -> Net-(U92-Pad5)
- U92 pad 6: (no net) -> Net-(U92-Pad6)
- U92 pad 7: (no net) -> Net-(U92-Pad7)
- U92 pad 8: (no net) -> Net-(U92-Pad8)
- U94 pad 1: (no net) -> Net-(U91-Pad5)
- U94 pad 2: (no net) -> Net-(U91-Pad6)
- U94 pad 3: (no net) -> Net-(U91-Pad7)
- U94 pad 4: (no net) -> Net-(U91-Pad8)
- U94 pad 5: (no net) -> Net-(U94-Pad5)
- U94 pad 6: (no net) -> Net-(U94-Pad6)
- U94 pad 7: (no net) -> Net-(U94-Pad7)
- U94 pad 8: (no net) -> Net-(U94-Pad8)
- U95 pad 1: (no net) -> Net-(U92-Pad5)
- U95 pad 2: (no net) -> Net-(U92-Pad6)
- U95 pad 3: (no net) -> Net-(U92-Pad7)
- U95 pad 4: (no net) -> Net-(U92-Pad8)
- U95 pad 5: (no net) -> Net-(U95-Pad5)
- U95 pad 6: (no net) -> Net-(U95-Pad6)
- U95 pad 7: (no net) -> Net-(U95-Pad7)
- U95 pad 8: (no net) -> Net-(U95-Pad8)
- U97 pad 1: (no net) -> Net-(U94-Pad5)
- U97 pad 2: (no net) -> Net-(U94-Pad6)
- U97 pad 3: (no net) -> Net-(U94-Pad7)
- U97 pad 4: (no net) -> Net-(U94-Pad8)
- U97 pad 5: (no net) -> Net-(U100-Pad1)
- U97 pad 6: (no net) -> Net-(U100-Pad2)
- U97 pad 7: (no net) -> Net-(U100-Pad3)
- U97 pad 8: (no net) -> Net-(U100-Pad4)
- U99 pad 1: (no net) -> Net-(U95-Pad5)
- U99 pad 2: (no net) -> Net-(U95-Pad6)
- U99 pad 3: (no net) -> Net-(U95-Pad7)
- U99 pad 4: (no net) -> Net-(U95-Pad8)
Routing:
- net Net-(U71-Pad8): track 0.00 -> 23.8 mm
